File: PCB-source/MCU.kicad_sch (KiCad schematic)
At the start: 38 parts, among them SW1 BOOT, SW2 RESET, U1 STM32F405RGTx, X1 X32258MOB4SI, X2 Q13FC1350000400

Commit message: ch32
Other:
- moved on the sheet: C26, C29, U1

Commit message: Component placement done
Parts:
- removed C405, C420, C421: 100nF, PCM_JLCPCB:C_0402, symbol PCM_JLCPCB-Capacitors:0402,100nF,(2)
- removed R400: 1.2kΩ, PCM_JLCPCB:R_0402, symbol PCM_JLCPCB-Resistors:0402,1.2kΩ
- removed R408: 220Ω, PCM_JLCPCB:R_0402, symbol PCM_JLCPCB-Resistors:0402,220Ω
- removed R409: 100Ω, PCM_JLCPCB:R_0402, symbol PCM_JLCPCB-Resistors:0402,100Ω
- added R23: 220Ω, PCM_JLCPCB:R_0402, symbol PCM_JLCPCB-Resistors:0402,220Ω
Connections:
- net Chainbus.MISO: now also U1.56 (PB4)
- net Chainbus.MOSI: now also U1.53 (PC12)
- net Chainbus.SCK: now also U1.55 (PB3)
- net Chainbus.SCL: now also U1.29 (PB10)
- net Chainbus.SDA: now also U1.30 (PB11)
- net Chainbus_I2C_addr0: now also U1.50 (PA15)
- net Chainbus_I2C_addr1: now also U1.57 (PB5)
- net Chainbus_I2C_addr2: now also U1.40 (PC9)
- net Chainbus_SPI_CS0: now also U1.37 (PC6)
- net Chainbus_SPI_CS1: now also U1.38 (PC7)
- net Chainbus_SPI_CS2: now also U1.39 (PC8)
- net Chainbus_UART_addr0: now also U1.22 (PA6)
- net Chainbus_UART_addr1: now also U1.23 (PA7)
- net Chainbus_UART_addr2: now also U1.21 (PA5)
- net USER_LED_1: now also R23.1
- net Altmode14: now reaches U1.10 (PC2)
- net Altmode15: now reaches U1.11 (PC3)
- net Altmode7: now reaches U1.14 (PA0)
- net Altmode8: now reaches U1.15 (PA1)
- net Altmode9: now reaches U1.16 (PA2)
- net Altmode10: now reaches U1.17 (PA3)
- net Altmode16: now reaches U1.24 (PC4)
- net Altmode4: now reaches U1.34 (PB13)
- net Altmode5: now reaches U1.35 (PB14)
- net Altmode6: now reaches U1.36 (PB15)
- net Altmode1: now reaches U1.41 (PA8)
- net Altmode2: now reaches U1.42 (PA9)
- net Altmode3: now reaches U1.43 (PA10)
- net Altmode11: now reaches U1.59 (PB7)
- net Altmode12: now reaches U1.8 (PC0)
- net Altmode13: now reaches U1.9 (PC1)
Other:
- note added: "ALTMODE HEADER"
- moved on the sheet: C422, C426

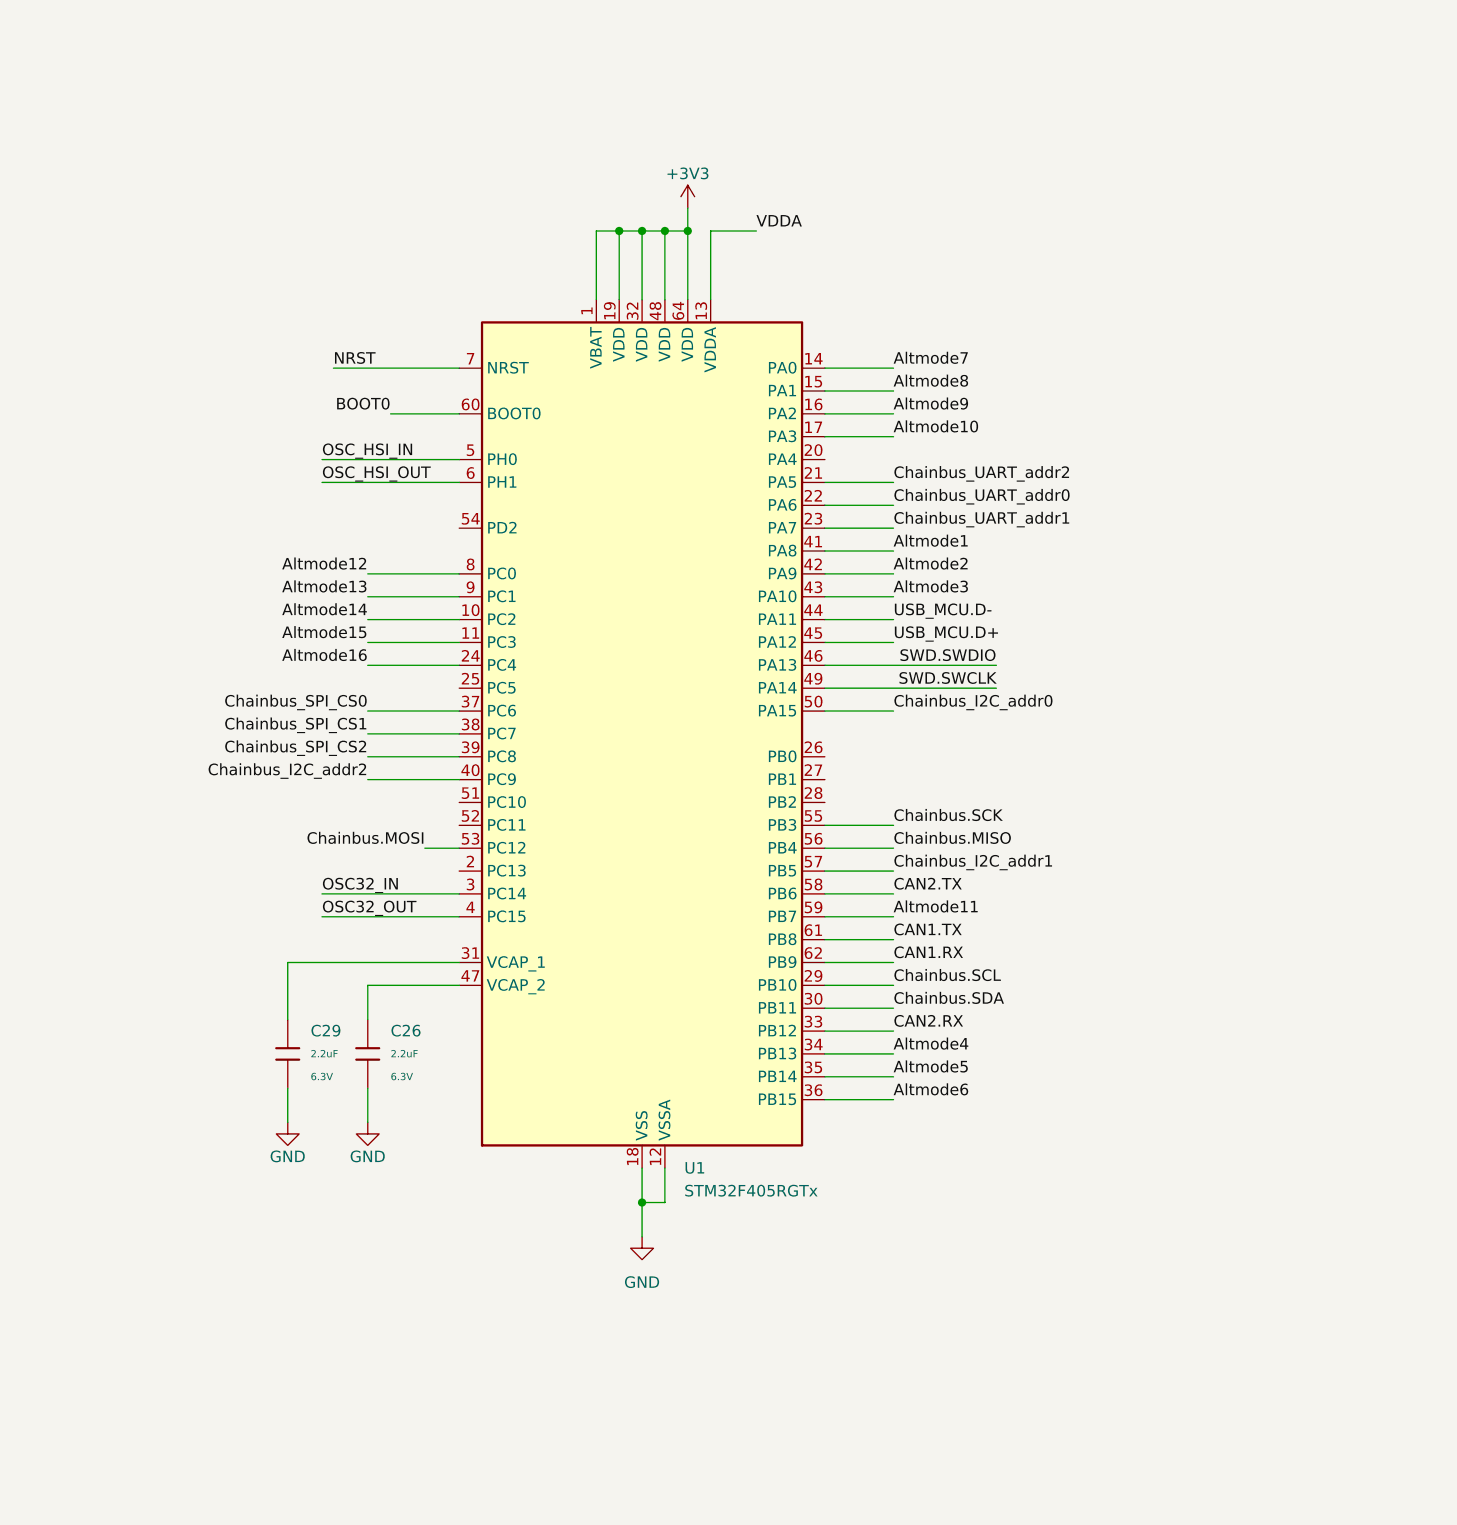
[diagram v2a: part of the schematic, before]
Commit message: processor connection done
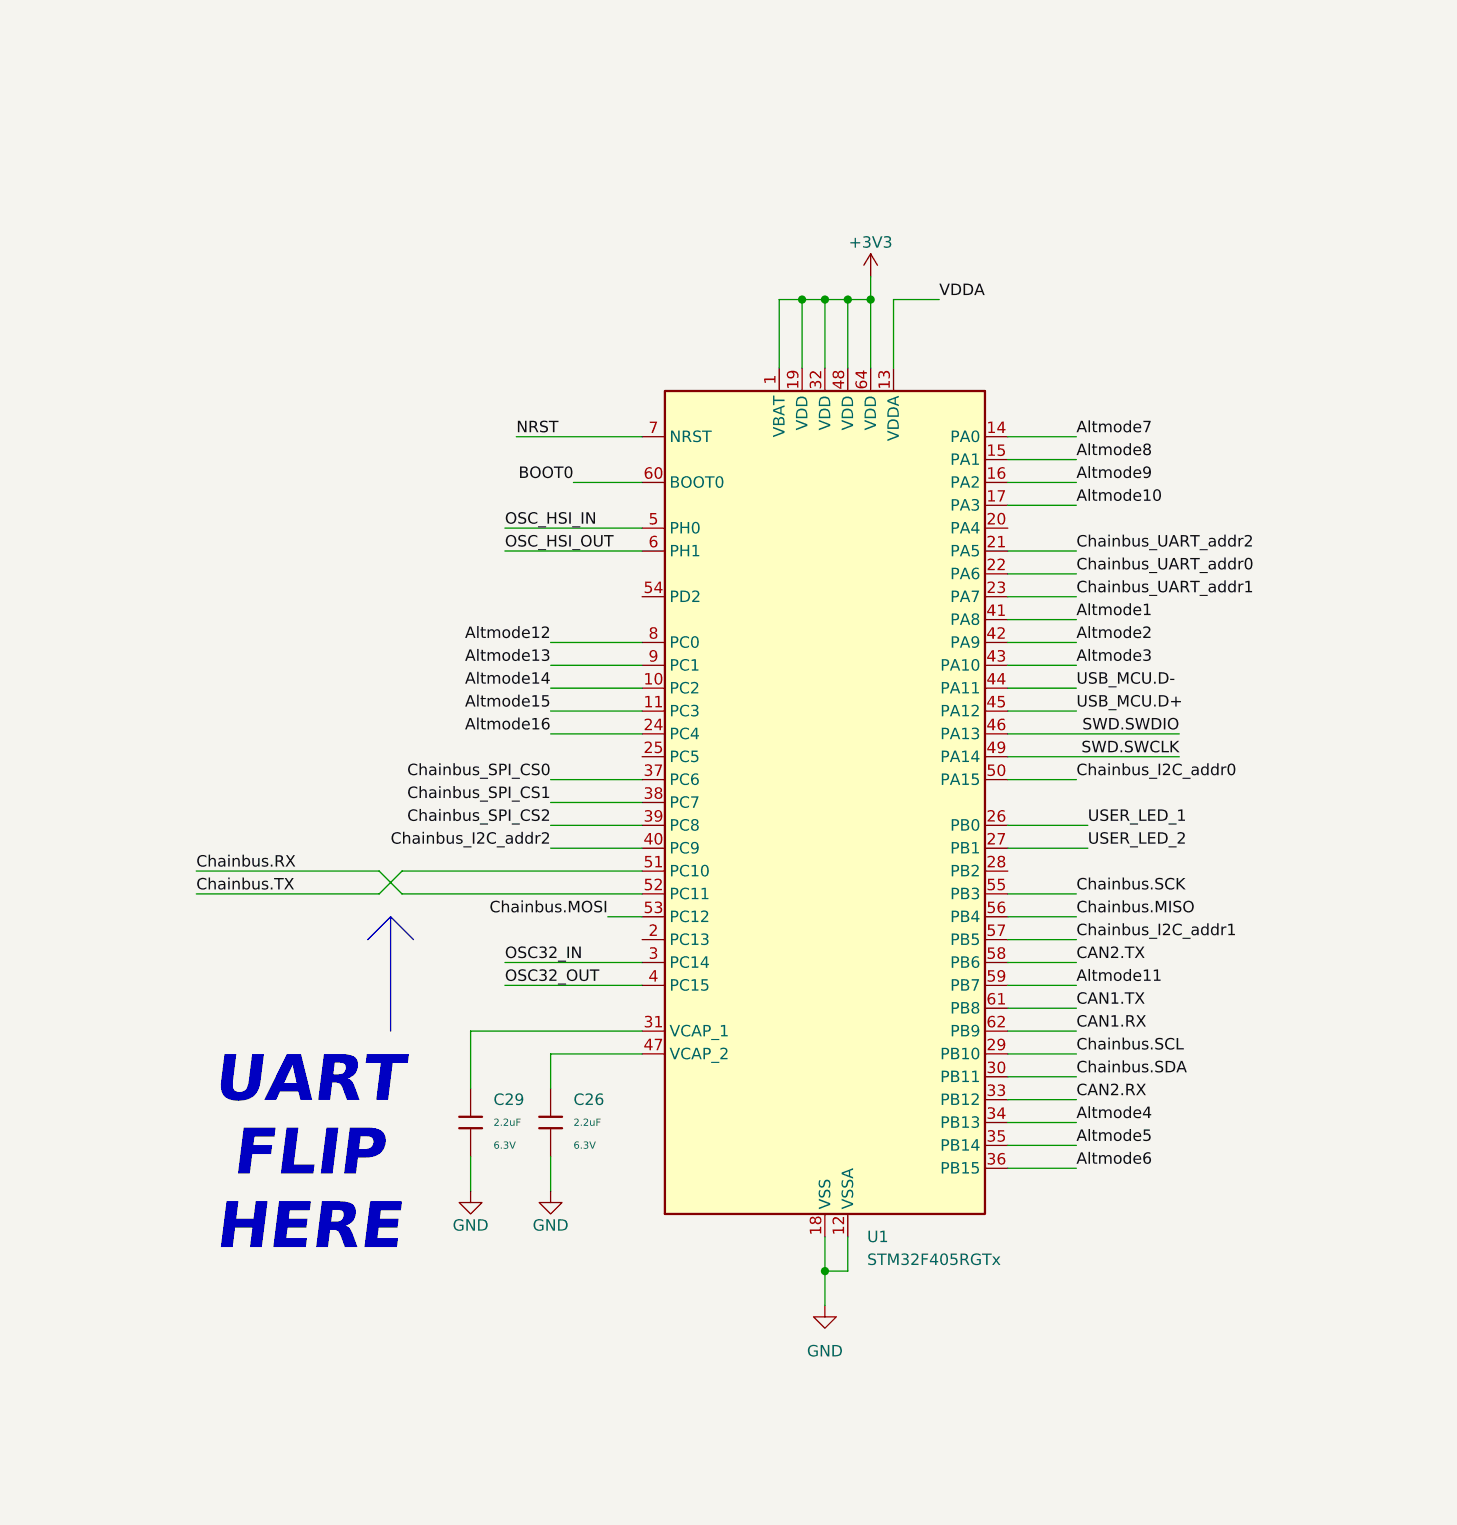
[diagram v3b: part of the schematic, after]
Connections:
- net Chainbus.RX: now also U1.52 (PC11)
- net Chainbus.TX: now also U1.51 (PC10)
- net USER_LED_1: now also U1.26 (PB0)
- net USER_LED_2: now also U1.27 (PB1)
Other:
- note added: "UART FLIP HERE"
- moved on the sheet: C26, C29, U1

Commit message: silk job, signal ratnest done
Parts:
- removed R23, R407: 220Ω, PCM_JLCPCB:R_0402, symbol PCM_JLCPCB-Resistors:0402,220Ω
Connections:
- net I2C_Memory_addr: now also U1.25 (PC5)

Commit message: change can term add usr led
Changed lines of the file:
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@@
 		)
 	)
-	(wire
+	(bus
 		(pts
-			(xy 370.84 31.75) (xy 370.84 34.29)
+			(xy 247.65 222.25) (xy 247.65 224.79)
 		)
 		(stroke
@@
 		)
 	)
-	(bus
+	(wire
 		(pts
-			(xy 247.65 222.25) (xy 247.65 224.79)
+			(xy 336.55 35.56) (xy 336.55 39.37)
 		)
 		(stroke
@@
 	(wire
 		(pts
-			(xy 364.49 31.75) (xy 370.84 31.75)
+			(xy 330.2 35.56) (xy 336.55 35.56)
 		)
 		(stroke
@@
 		)
 	)
+	(wire
+		(pts
+			(xy 367.03 39.37) (xy 361.95 39.37)
+		)
+		(stroke
+			(width 0)
+			(type default)
+		)
+	)
 	(bus
 		(pts
@@
 	(wire
 		(pts
+			(xy 341.63 39.37) (xy 336.55 39.37)
+		)
+		(stroke
+			(width 0)
+			(type default)
+		)
+	)
+	(wire
+		(pts
 			(xy 236.22 54.61) (xy 238.76 54.61)
 		)
@@
 	(wire
 		(pts
-			(xy 387.35 34.29) (xy 387.35 31.75)
+			(xy 361.95 35.56) (xy 361.95 39.37)
 		)
 		(stroke
@@
 	(wire
 		(pts
-			(xy 381 31.75) (xy 387.35 31.75)
+			(xy 355.6 35.56) (xy 361.95 35.56)
 		)
 		(stroke
@@
 	)
 	(label "USER_LED_1"
-		(at 364.49 31.75 0)
+		(at 330.2 35.56 0)
 		(effects
 			(font
@@
 	)
 	(label "USER_LED_2"
-		(at 381 31.75 0)
+		(at 355.6 35.56 0)
 		(effects
 			(font
@@
 		)
 	)
+	(hierarchical_label "USER_LED_2"
+		(shape input)
+		(at 367.03 39.37 0)
+		(effects
+			(font
+				(size 1.27 1.27)
+			)
+			(justify left)
+		)
+	)
 	(hierarchical_label "USB_MCU{USB}"
 		(shape input)
@@
 		(effects
 			(font
+				(size 1.27 1.27)
+			)
+			(justify left)
+		)
+	)
+	(hierarchical_label "USER_LED_1"
+		(shape input)
+		(at 341.63 39.37 0)
+		(effects
+			(font

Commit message: DRC PASS, preparing bom for production
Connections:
- net USER_LED_1: now also U1.27 (PB1); no longer U1.26 (PB0)
- net USER_LED_2: now also U1.26 (PB0); no longer U1.27 (PB1)
- net USR_BUTTON: now also U1.54 (PD2)
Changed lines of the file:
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@@
 	(wire
 		(pts
+			(xy 214.63 87.63) (xy 220.98 87.63)
+		)
+		(stroke
+			(width 0)
+			(type default)
+		)
+	)
+	(wire
+		(pts
 			(xy 386.08 181.61) (xy 386.08 184.15)
 		)
@@
 		)
 	)
-	(label "USER_LED_2"
-		(at 270.51 115.57 0)
-		(effects
-			(font
-				(size 1.27 1.27)
-			)
-			(justify left bottom)
-		)
-	)
 	(label "BOOT0"
 		(at 85.09 85.09 180)
@@
 		)
 	)
-	(label "USER_LED_1"
-		(at 270.51 113.03 0)
-		(effects
-			(font
-				(size 1.27 1.27)
-			)
-			(justify left bottom)
-		)
-	)
 	(label "Chainbus.TX"
 		(at 113.03 173.99 0)
@@
 		)
 	)
+	(label "USER_LED_2"
+		(at 270.51 113.03 0)
+		(effects
+			(font
+				(size 1.27 1.27)
+			)
+			(justify left bottom)
+		)
+	)
 	(label "Altmode3"
 		(at 269.24 95.25 0)
@@
 		)
 	)
+	(label "USR_BUTTON"
+		(at 214.63 87.63 180)
+		(effects
+			(font
+				(size 1.27 1.27)
+			)
+			(justify right bottom)
+		)
+	)
 	(label "Chainbus_SPI_CS2"
 		(at 241.3 255.27 180)
@@
 		(effects
 			(font
+				(size 1.27 1.27)
+			)
+			(justify left bottom)
+		)
+	)
+	(label "USER_LED_1"
+		(at 270.51 115.57 0)
+		(effects
+			(font

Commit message: bom done
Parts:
- C410, R401: now not fitted
- SW1, SW2: LCSC C2888954 -> C22375371
- U1: LCSC (none) -> C15742
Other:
- note added: "ALTERNATE PART: APM32F405RGT6 - C5290473 CKS32F405RGT6 - C5185730 GD32F405RGT6 - C99031"
- note added: "NOTE:"
- note added: "REV A. NC"
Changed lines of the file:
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@@
 	)
 	(rectangle
+		(start 271.78 170.18)
+		(end 316.23 175.26)
+		(stroke
+			(width 0)
+			(type default)
+		)
+		(fill
+			(type none)
+		)
+	)
+	(rectangle
 		(start 293.37 210.82)
 		(end 350.52 247.65)
@@
 	)
 	(rectangle
+		(start 271.78 175.26)
+		(end 316.23 187.96)
+		(stroke
+			(width 0)
+			(type default)
+		)
+		(fill
+			(type none)
+		)
+	)
+	(rectangle
 		(start 354.33 101.6)
 		(end 402.59 152.4)
@@
 		)
 	)
+	(text "NOTE:"
+		(exclude_from_sim no)
+		(at 272.288 172.974 0)
+		(effects
+			(font
+				(size 2.54 2.54)
+				(thickness 0.254)
+				(bold yes)
+			)
+			(justify left)
+		)
+	)
 	(text "CHAINBUS UART\n"
 		(exclude_from_sim no)
@@
 		)
 	)
+	(text "ALTERNATE PART:\nAPM32F405RGT6 - C5290473\nCKS32F405RGT6 - C5185730\nGD32F405RGT6  - C99031"
+		(exclude_from_sim no)
+		(at 272.542 181.61 0)
+		(effects
+			(font
+				(size 1.27 1.27)
+				(thickness 0.254)
+				(bold yes)
+				(color 255 45 78 1)
+			)
+			(justify left)
+		)
+	)
 	(text "RESET BUTTON"
 		(exclude_from_sim no)
@@
 		)
 	)
+	(text "REV A. NC"
+		(exclude_from_sim no)
+		(at 116.078 88.392 0)
+		(effects
+			(font
+				(size 1.27 1.27)
+			)
+		)
+	)
 	(text "CRYSTAL RESONATORS"
 		(exclude_from_sim no)
@@
 		(in_bom yes)
 		(on_board yes)
-		(dnp no)
+		(dnp yes)
 		(property "Reference" "C410"
 			(at 86.868 88.9 0)
@@
 			)
 		)
-		(property "LCSC" " C2888954"
+		(property "LCSC" "C22375371"
 			(at 48.26 185.42 0)
 			(effects
@@
 			)
 		)
-		(property "LCSC" " C2888954"
+		(property "LCSC" "C22375371"
 			(at 53.34 144.78 0)
 			(effects
@@
 			)
 		)
+		(property "LCSC" "C15742"
+			(at 241.3 110.49 0)
+			(effects
+				(font
+					(size 1.27 1.27)
+				)
+				(hide yes)
+			)
+		)
 		(pin "52"
 		)
@@
 		(in_bom yes)
 		(on_board yes)
-		(dnp no)
+		(dnp yes)
 		(property "Reference" "R401"
 			(at 67.31 82.804 90)
